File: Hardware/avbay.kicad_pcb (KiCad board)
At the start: 2 copper layers, 30.5 x 83.2 mm, 63 parts, among them P1 TERM_BLOCK_2.54MM_2POS, P2 CONN_6, P3 TERM_BLOCK_2.54MM_8POS, P4 TERM_BLOCK_2.54MM_5POS, P5 TERM_BLOCK_2.54MM_5POS, P6 TERM_BLOCK_2.54MM_2POS, P7 TERM_BLOCK_2.54MM_8POS, P8 CONN_01X02, Q1 DMN2041LSD, Q2 BSS138DW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

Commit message: Fixed a via that was dumb
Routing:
- net GND: track 396.4 -> 396.2 mm, vias 26 -> 24

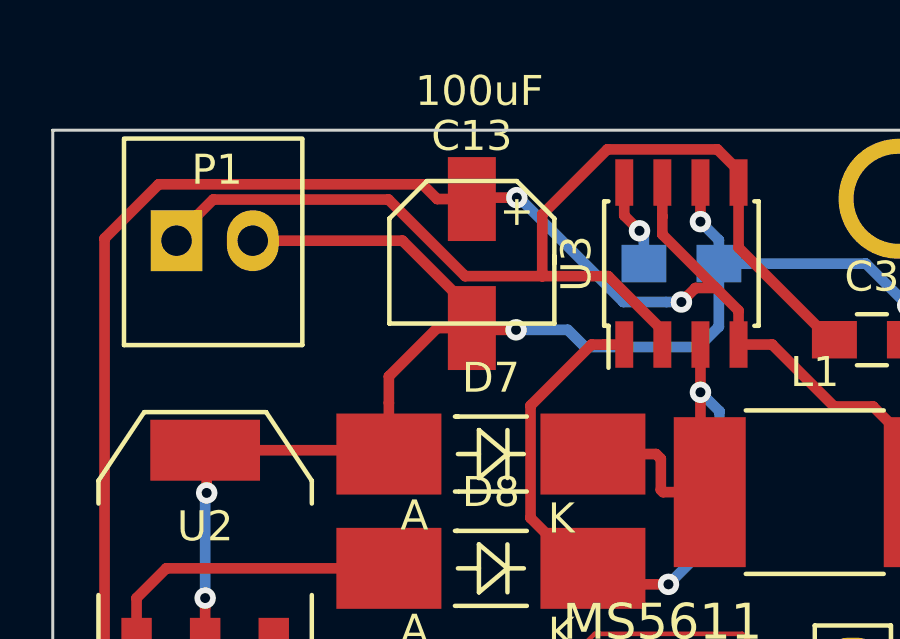
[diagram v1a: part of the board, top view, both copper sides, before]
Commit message: Switched to tantalum capacitor for power supply
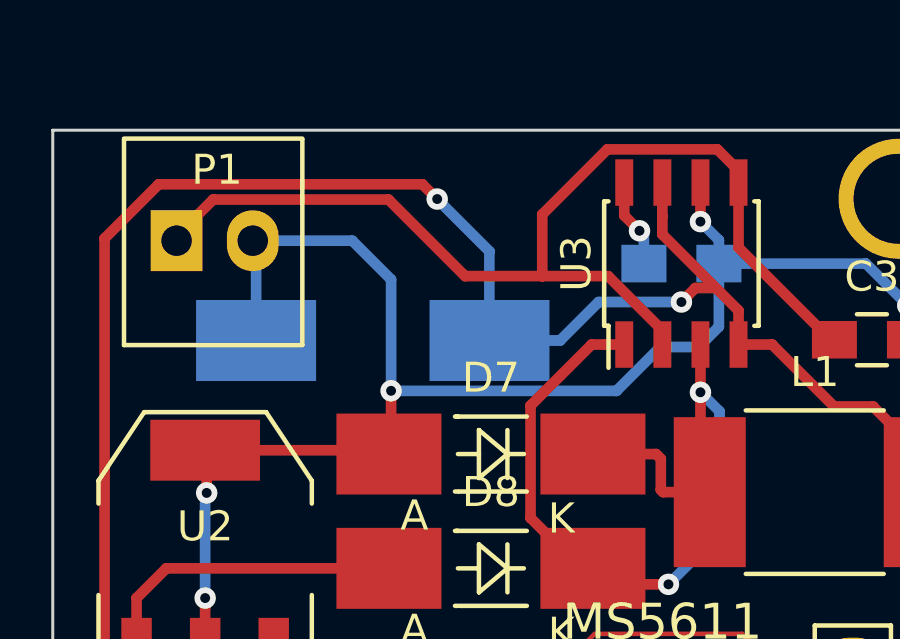
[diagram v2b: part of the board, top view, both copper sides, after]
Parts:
- C13: footprint Local:SMD_CAP -> Capacitors_Tantalum_SMD:TantalC_SizeD_EIA-7343_HandSoldering; moved to B.Cu
- moved C13 4.18 mm to (147.8, 50.2), turned to 180 degrees
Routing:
- net GND: track 396.2 -> 399.9 mm
- net +5V: track 147.2 -> 150.0 mm

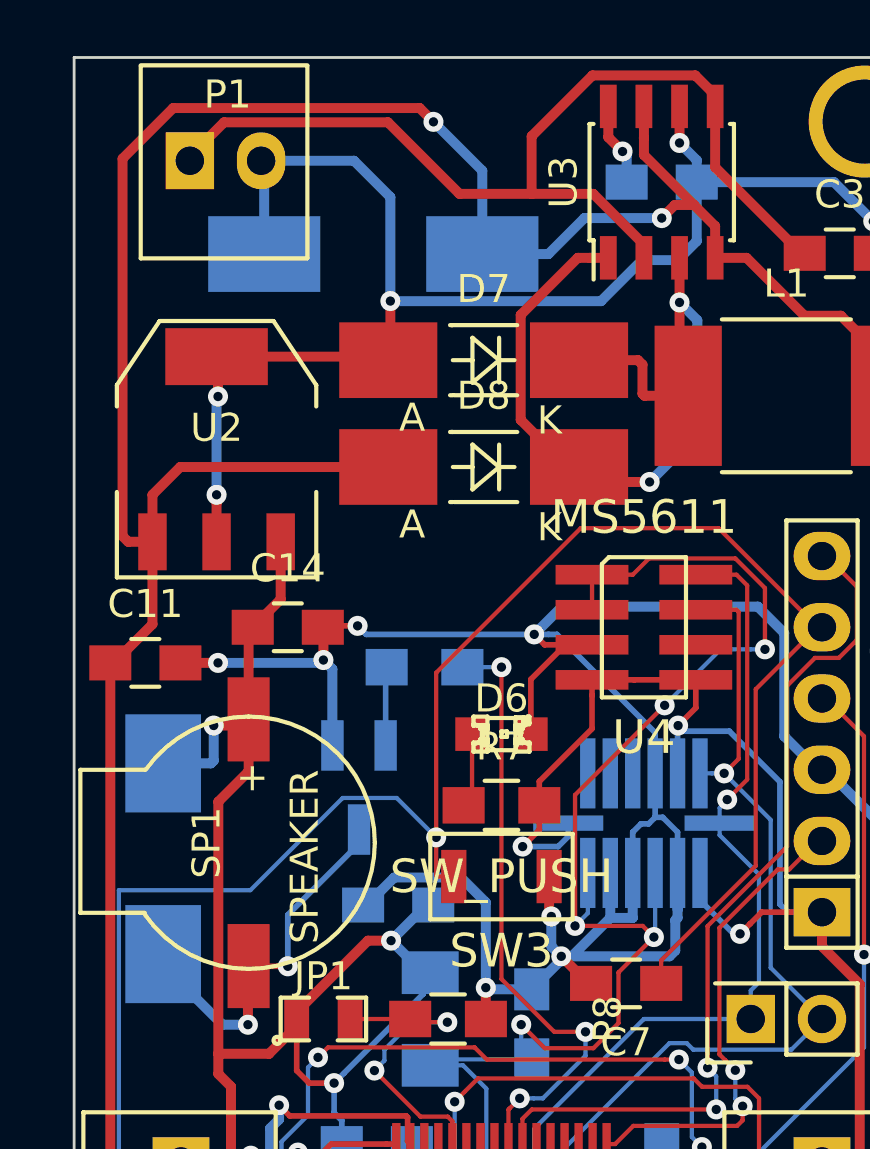
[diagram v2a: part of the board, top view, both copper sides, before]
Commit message: Added MicroSD card
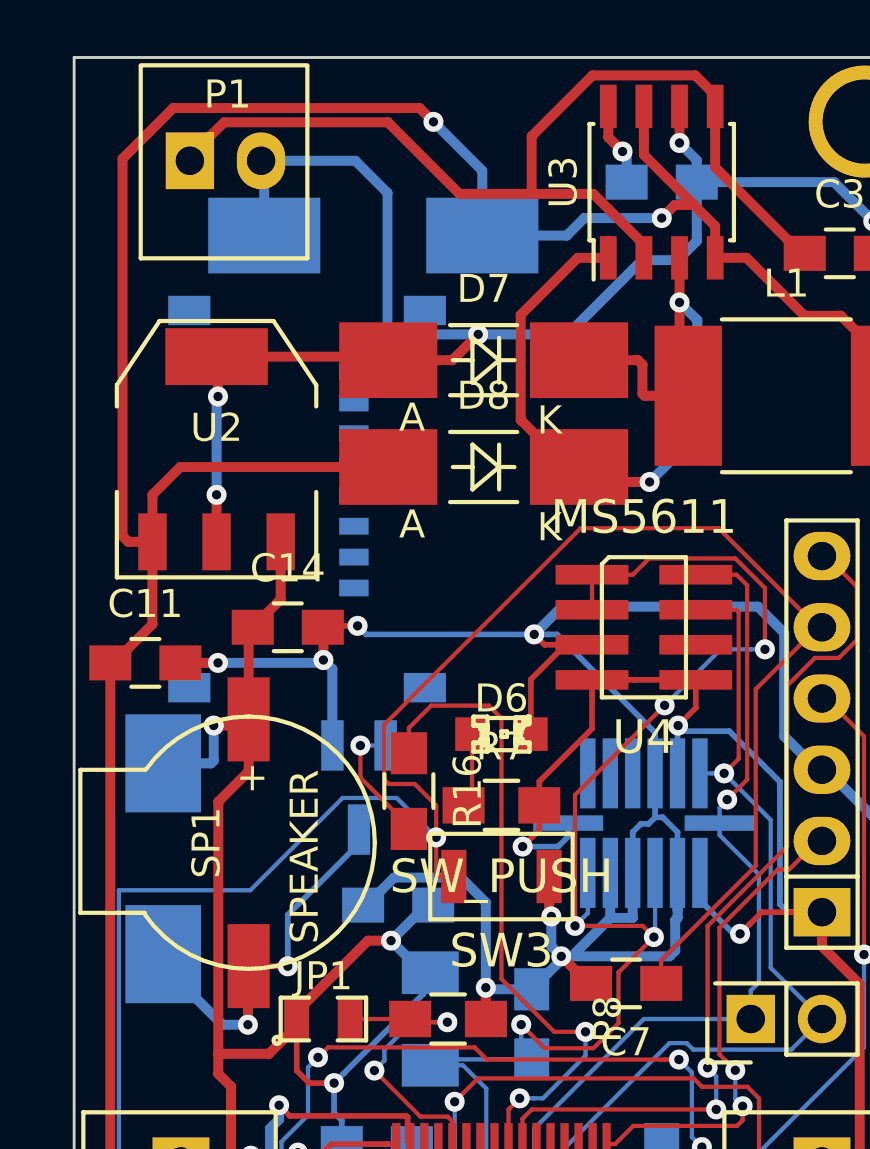
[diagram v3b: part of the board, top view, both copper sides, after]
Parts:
- added J1: MicroSD, Ian:MICRO_SD_HINGE_AMP, B.Cu at (137.7, 58.9)
- R16: moved to F.Cu
- moved R16 4.45 mm to (149.1, 69.3), turned to 270 degrees
- moved C13 0.66 mm to (147.8, 49.5)
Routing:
- net GND: track 399.9 -> 402.6 mm
- net /MCU/NRST: track 74.5 -> 76.6 mm
- net Net-(Q5-Pad2): track 2.81 -> 4.59 mm, vias 0 -> 1
- net /MCU/GPIO4: track 21.9 -> 23.4 mm, vias 3 -> 2
- net +5V: track 150.0 -> 149.1 mm

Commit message: Fixed routing
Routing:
- net /Sensors/ACCEL_INT_1: track 0.00 -> 25.5 mm, vias 0 -> 3
- net /Sensors/ACCEL_INT_2: track 0.00 -> 20.4 mm, vias 0 -> 3
- net GND: track 402.6 -> 407.0 mm
- net 3V3: track 210.5 -> 214.5 mm
- net /MCU/VDDA: track 62.5 -> 64.2 mm
- net /MCU/GPIO4: track 23.4 -> 22.1 mm
- net /Sensors/SCL: track 34.8 -> 33.9 mm
- net /MCU/RADIO_RX: track 34.3 -> 35.1 mm
